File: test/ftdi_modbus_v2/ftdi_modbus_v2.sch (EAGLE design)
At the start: 31 parts, among them IC1 FT232RL, IC2 SP483E, J1 CLIFF_DCJACK2.1-2.5MM, J2 MB_CONN

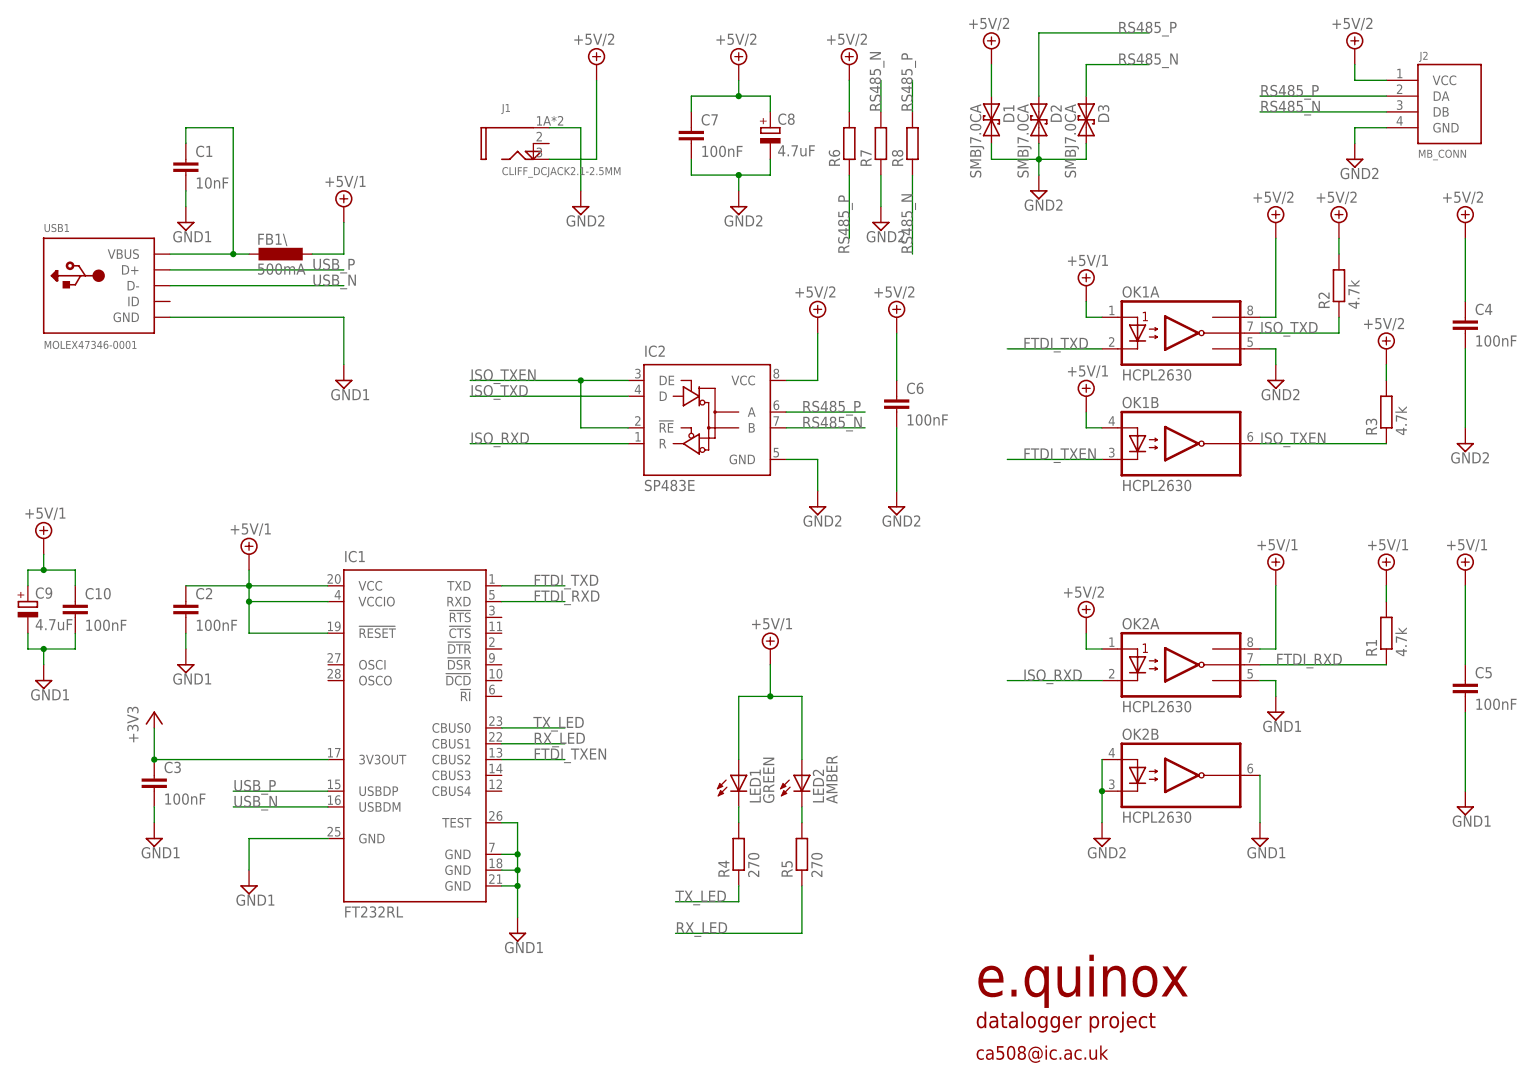
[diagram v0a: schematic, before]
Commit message: Created ftdi_modbus_v2 layout
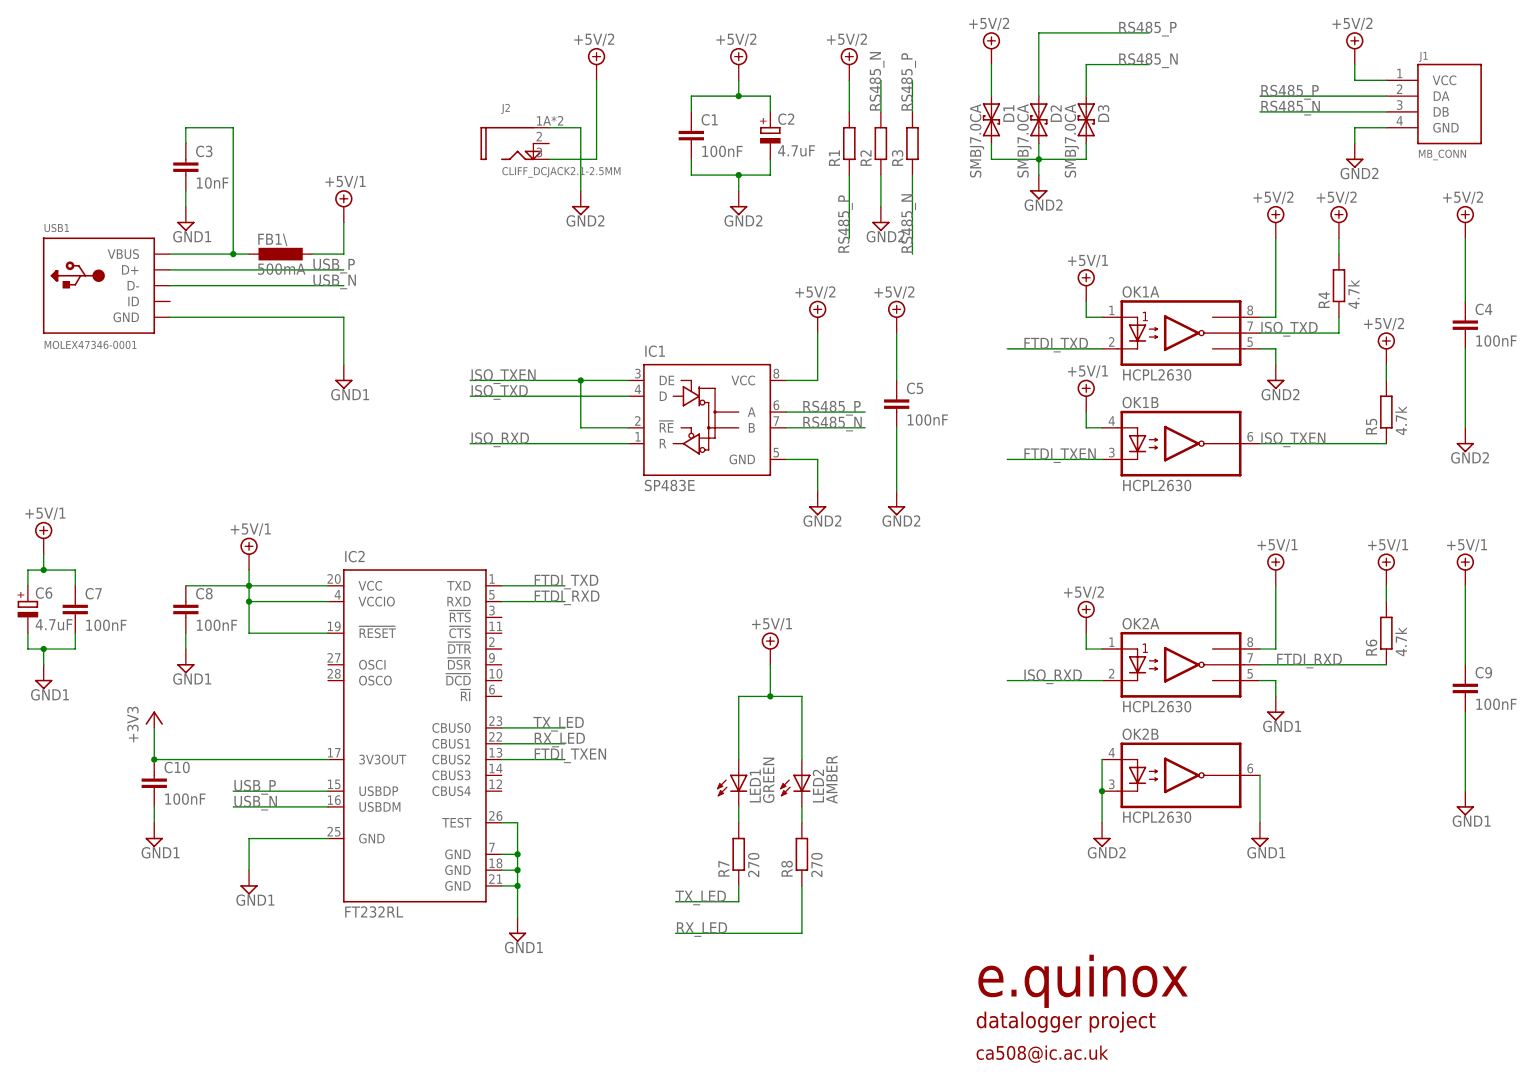
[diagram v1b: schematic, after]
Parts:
- C1: value 10nF -> 100nF
- C2, C6: value 100nF -> 4.7uF; device resistor:C-EUC0603 -> resistor:CPOL-EUB/3528-21R
- C3: value 100nF -> 10nF
- C5: device resistor:C-EUC1206 -> resistor:C-EUC0603
- C8: value 4.7uF -> 100nF; device resistor:CPOL-EUB/3528-21R -> resistor:C-EUC0603
- C9: value 4.7uF -> 100nF; device resistor:CPOL-EUB/3528-21R -> resistor:C-EUC1206
- IC1: value FT232RL -> SP483E; device ftdichip:FT232RL -> 751xx:75176AD
- IC2: value SP483E -> FT232RL; device 751xx:75176AD -> ftdichip:FT232RL
- J1: value CLIFF_DCJACK2.1-2.5MM -> MB_CONN; device minibox-parts:CLIFF_DCJACK2.1-2.5MM -> connectors-pheonix:MB_CONN
- J2: value MB_CONN -> CLIFF_DCJACK2.1-2.5MM; device connectors-pheonix:MB_CONN -> minibox-parts:CLIFF_DCJACK2.1-2.5MM
- R1, R2, R3: value 4.7k -> (none); device resistor:R-EU_M0805 -> resistor:R-EU_0207/10
- R4, R5: value 270 -> 4.7k
- R6: value (none) -> 4.7k; device resistor:R-EU_0207/10 -> resistor:R-EU_M0805
- R7, R8: value (none) -> 270; device resistor:R-EU_0207/10 -> resistor:R-EU_M0805
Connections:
- net +3V3: now also C10.1, IC2.3V3OUT; no longer C3.1, IC1.3V3OUT
- net +5V/1: now also C6.+, C7.1, C8.1, C9.1, IC2.!RESET, IC2.VCC, IC2.VCCIO, R6.2; no longer C10.1, C2.1, C5.1, C9.+, IC1.!RESET, IC1.VCC, IC1.VCCIO, R1.2
- net +5V/2: now also C1.1, C2.+, C5.1, IC1.VCC, J1.VCC, J2.TIP, R1.2, R4.2, R5.2; no longer C6.1, C7.1, C8.+, IC2.VCC, J1.TIP, J2.VCC, R2.2, R3.2, R6.2
- net FTDI_RXD: now also IC2.RXD, R6.1; no longer IC1.RXD, R1.1
- net FTDI_TXD: now also IC2.TXD; no longer IC1.TXD
- net FTDI_TXEN: now also IC2.CBUS2; no longer IC1.CBUS2
- net GND1: now also C6.-, C7.2, C8.2, C9.2, IC2.GND, IC2.GND@1, IC2.GND@2, IC2.GND@A, IC2.TEST; no longer C1.2, C2.2, C5.2, C9.-, IC1.GND, IC1.GND@1, IC1.GND@2, IC1.GND@A, IC1.TEST
- net GND2: now also C1.2, C2.-, C5.2, IC1.GND, J1.GND, J2.SLEEVE, R2.1; no longer C6.2, C7.2, C8.-, IC2.GND, J1.SLEEVE, J2.GND, R7.1
- net ISO_RXD: now also IC1.R; no longer IC2.R
- net ISO_TXD: now also IC1.D, R4.1; no longer IC2.D, R2.1
- net ISO_TXEN: now also IC1.!RE, IC1.DE, R5.1; no longer IC2.!RE, IC2.DE, R3.1
- net N$1: now also C3.1; no longer C1.1
- net N$3: now also R7.2; no longer R4.2
- net N$4: now also R8.2; no longer R5.2
- net RS485_N: now also IC1.B, J1.DB, R2.2, R3.1; no longer IC2.B, J2.DB, R7.2, R8.1
- net RS485_P: now also IC1.A, J1.DA, R1.1, R3.2; no longer IC2.A, J2.DA, R6.1, R8.2
- net RX_LED: now also IC2.CBUS1, R8.1; no longer IC1.CBUS1, R5.1
- net TX_LED: now also IC2.CBUS0, R7.1; no longer IC1.CBUS0, R4.1
- net USB_N: now also IC2.USBDM; no longer IC1.USBDM
- net USB_P: now also IC2.USBDP; no longer IC1.USBDP
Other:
- moved on the sheet: C1, C10, C3, C5, C7, R1, R2, R3, R4, R5, R6, R7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

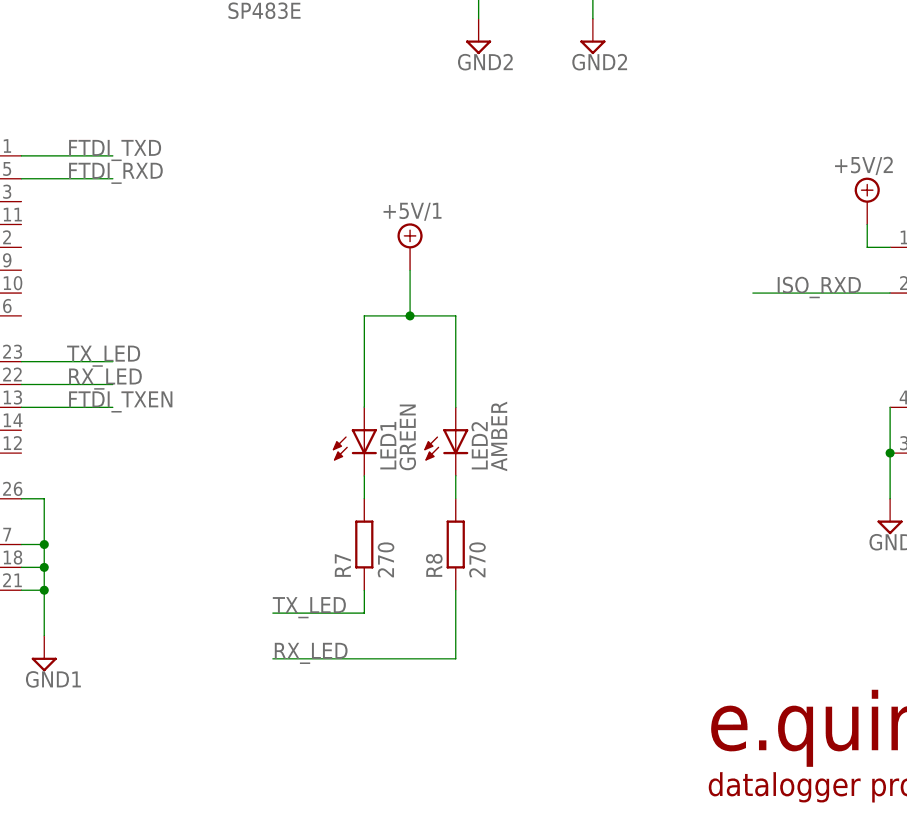
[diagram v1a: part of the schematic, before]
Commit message: Completed layout of ftdi_rs485_v2 test board. Added more status LEDs
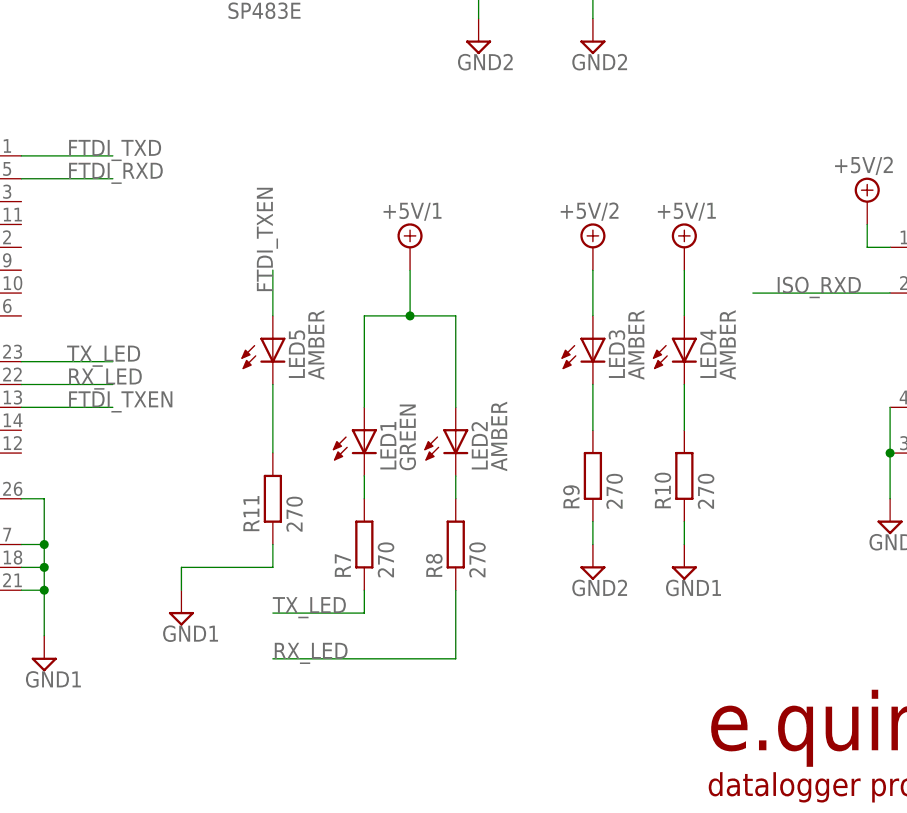
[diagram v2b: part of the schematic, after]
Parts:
- added LED3, LED4, LED5: AMBER, led:LEDCHIPLED_0805
- added R10, R11, R9: 270, resistor:R-EU_M0805
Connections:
- new net N$7: LED3.C, R9.2
- new net N$8: LED4.C, R10.2
- new net N$9: LED5.C, R11.2
- net +5V/1: now also LED4.A
- net +5V/2: now also LED3.A
- net FTDI_TXEN: now also LED5.A
- net GND1: now also R10.1, R11.1
- net GND2: now also R9.1
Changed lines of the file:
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@@
 <part name="SUPPLY40" library="supply2" deviceset="+5V/2" device=""/>
 <part name="SUPPLY41" library="supply2" deviceset="GND2" device=""/>
+<part name="LED3" library="led" deviceset="LED" device="CHIPLED_0805" value="AMBER"/>
+<part name="R9" library="resistor" deviceset="R-EU_" device="M0805" value="270"/>
+<part name="SUPPLY42" library="supply2" deviceset="+5V/2" device=""/>
+<part name="SUPPLY43" library="supply2" deviceset="GND2" device=""/>
+<part name="LED4" library="led" deviceset="LED" device="CHIPLED_0805" value="AMBER"/>
+<part name="R10" library="resistor" deviceset="R-EU_" device="M0805" value="270"/>
+<part name="SUPPLY44" library="supply2" deviceset="GND1" device=""/>
+<part name="SUPPLY45" library="supply2" deviceset="+5V/1" device=""/>
+<part name="R11" library="resistor" deviceset="R-EU_" device="M0805" value="270"/>
+<part name="LED5" library="led" deviceset="LED" device="CHIPLED_0805" value="AMBER"/>
+<part name="SUPPLY46" library="supply2" deviceset="GND1" device=""/>
 </parts>
 <sheets>
@@
 <instance part="SUPPLY40" gate="G$1" x="144.78" y="165.1"/>
 <instance part="SUPPLY41" gate="G$1" x="149.86" y="139.7"/>
+<instance part="LED3" gate="G$1" x="152.4" y="60.96"/>
+<instance part="R9" gate="G$1" x="152.4" y="45.72" rot="R90"/>
+<instance part="SUPPLY42" gate="G$1" x="152.4" y="71.12"/>
+<instance part="SUPPLY43" gate="G$1" x="152.4" y="35.56"/>
+<instance part="LED4" gate="G$1" x="162.56" y="60.96"/>
+<instance part="R10" gate="G$1" x="162.56" y="45.72" rot="R90"/>
+<instance part="SUPPLY44" gate="G$1" x="162.56" y="35.56"/>
+<instance part="SUPPLY45" gate="G$1" x="162.56" y="71.12"/>
+<instance part="R11" gate="G$1" x="116.84" y="43.18" rot="R90"/>
+<instance part="LED5" gate="G$1" x="116.84" y="60.96"/>
+<instance part="SUPPLY46" gate="G$1" x="106.68" y="30.48"/>
 </instances>
 <busses>
@@
 <junction x="15.24" y="71.12"/>
 </segment>
+<segment>
+<pinref part="SUPPLY44" gate="G$1" pin="GND1"/>
+<pinref part="R10" gate="G$1" pin="1"/>
+<wire x1="162.56" y1="38.1" x2="162.56" y2="40.64" width="0.1524" layer="91"/>
+</segment>
+<segment>
+<pinref part="R11" gate="G$1" pin="1"/>
+<wire x1="116.84" y1="38.1" x2="116.84" y2="35.56" width="0.1524" layer="91"/>
+<wire x1="116.84" y1="35.56" x2="106.68" y2="35.56" width="0.1524" layer="91"/>
+<wire x1="106.68" y1="35.56" x2="106.68" y2="33.02" width="0.1524" layer="91"/>
+<pinref part="SUPPLY46" gate="G$1" pin="GND1"/>
+</segment>
 </net>
 <net name="USB_P" class="0">
@@
 <junction x="15.24" y="83.82"/>
 </segment>
+<segment>
+<pinref part="LED4" gate="G$1" pin="A"/>
+<pinref part="SUPPLY45" gate="G$1" pin="+5V/1"/>
+<wire x1="162.56" y1="63.5" x2="162.56" y2="68.58" width="0.1524" layer="91"/>
+</segment>
 </net>
 <net name="N$1" class="0">
@@
 <label x="172.72" y="101.6" size="1.778" layer="95"/>
 </segment>
+<segment>
+<pinref part="LED5" gate="G$1" pin="A"/>
+<wire x1="116.84" y1="63.5" x2="116.84" y2="68.58" width="0.1524" layer="91"/>
+<label x="116.84" y="66.04" size="1.778" layer="95" rot="R90"/>
+</segment>
 </net>
 <net name="RX_LED" class="0">
@@
 <pinref part="SUPPLY40" gate="G$1" pin="+5V/2"/>
 <wire x1="144.78" y1="157.48" x2="144.78" y2="162.56" width="0.1524" layer="91"/>
+</segment>
+<segment>
+<pinref part="LED3" gate="G$1" pin="A"/>
+<pinref part="SUPPLY42" gate="G$1" pin="+5V/2"/>
+<wire x1="152.4" y1="68.58" x2="152.4" y2="63.5" width="0.1524" layer="91"/>
 </segment>
 </net>
@@
 <wire x1="149.86" y1="142.24" x2="149.86" y2="147.32" width="0.1524" layer="91"/>
 </segment>
+<segment>
+<pinref part="R9" gate="G$1" pin="1"/>
+<pinref part="SUPPLY43" gate="G$1" pin="GND2"/>
+<wire x1="152.4" y1="40.64" x2="152.4" y2="38.1" width="0.1524" layer="91"/>
+</segment>
 </net>
 <net name="ISO_TXD" class="0">
@@
 </segment>
 </net>
+<net name="N$7" class="0">
+<segment>
+<pinref part="LED3" gate="G$1" pin="C"/>
+<pinref part="R9" gate="G$1" pin="2"/>
+<wire x1="152.4" y1="55.88" x2="152.4" y2="50.8" width="0.1524" layer="91"/>
+</segment>
+</net>
+<net name="N$8" class="0">
+<segment>
+<pinref part="R10" gate="G$1" pin="2"/>
+<pinref part="LED4" gate="G$1" pin="C"/>
+<wire x1="162.56" y1="50.8" x2="162.56" y2="55.88" width="0.1524" layer="91"/>
+</segment>
+</net>
+<net name="N$9" class="0">
+<segment>
+<pinref part="R11" gate="G$1" pin="2"/>
+<wire x1="116.84" y1="48.26" x2="116.84" y2="55.88" width="0.1524" layer="91"/>
+<pinref part="LED5" gate="G$1" pin="C"/>
+</segment>
+</net>
